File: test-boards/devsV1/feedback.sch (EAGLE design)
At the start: 5 parts, among them IC1 TL074P, Q1 BD139, Q2 BD140

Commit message: feedback schematic transfer done
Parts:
- added C10, C7: 0.1uF, rcl:C-EU025-030X050
- added C11, C8: 22nF, rcl:C-EU025-030X050
- added C12, C9: 220n, rcl:C-EU025-030X050
- added C13, C14: 50n, rcl:C-EU025-030X050
- added C2, C5: 0.33uF, rcl:C-EU025-030X050
- added C3, C6: 1uF, rcl:C-EU025-030X050
- added C4: 2.2 uF, rcl:CPOL-EUE2-5
- added D1, D2, D3, D4, D5, D6, D7: 1N4148, BeagleBone_Blue_R3:DIODE1N4148
- added IC2: 7805L, adafruit:7805L
- added IC3: 7905L, linear:7905L
- added IC4, IC5: TL074P, linear:TL074P
- added JP1, JP2, JP3, JP4, JP5, JP6, JP7: 1x2, pinhead:PINHD-1X2
- added R10, R18: 620K, resistor:R-EU_0207/10
- added R11, R13, R22, R24, R3, R30, R32, R33, R34, R41, R42, R5: 10K, resistor:R-EU_0207/10
- added R12, R14, R17, R4, R6, R9: 1M, resistor:R-EU_0207/10
- added R15, R19, R2, R20, R21, R27, R28, R29, R36, R37, R38, R39, R44, R45, R7: 100K, resistor:R-EU_0207/10
- added R16, R50, R8: 20K, resistor:R-EU_0207/10
- added R23, R31: 300K, resistor:R-EU_0207/10
- added R25, R35, R48, R49: 15K, resistor:R-EU_0207/10
- added R26, R40: 50K, resistor:R-EU_0207/10
- added R43: 150K, resistor:R-EU_0207/10
- added R46: 120K, resistor:R-EU_0207/10
- added R47: 1K, resistor:R-EU_0207/10
- added T1: (no value), transistor:BC337-25-NPN-TO92-CBE
- C1: value (none) -> 2.2 uF
- R1: value (none) -> 100K
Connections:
- new net +12V: JP2.1, Q1.C, R1.1
- new net -12V: JP3.2, Q2.C, R2.1
- new net GND: C1.-, C10.2, C12.1, C2.2, C3.2, C4.-, C5.2, C6.2, C7.2, C9.1, D2.A, D4.A, IC2.GND, IC3.GND, IC4C.+IN, IC4D.+IN, IC5C.+IN, JP1.2, JP2.2, JP3.1, JP4.1, JP5.2, JP6.1, JP7.2, R10.1, R14.1, R15.1, R18.1, R22.2, R24.2, R30.2, R32.2, R39.2, R41.2, R42.2, R49.2, R6.1, R7.1, T1.E
- new net INH: C13.2, IC4D.OUT, JP5.1, R26.1, R47.2
- new net N$1: C1.+, Q1.B, R1.2
- new net N$10: C10.1, IC1B.-IN, R11.2, R12.1
- new net N$11: C9.2, D2.C, IC1D.-IN, R8.2
- new net N$12: D1.C, IC1D.+IN, R10.2, R9.1
- new net N$13: IC1D.OUT, R20.2, R8.1, R9.2
- new net N$14: R36.2, R39.1, R40.1
- new net N$15: IC4A.-IN, R22.1, R23.2
- new net N$16: IC1B.+IN, R13.1, R14.2
- new net N$17: C11.2, D3.A, R15.2
- new net N$18: C12.2, D4.C, IC1C.+IN, R16.2
- new net N$19: IC1C.OUT, R16.1, R17.2, R28.2
- new net N$2: C2.1, IC2.VI, Q1.E
- new net N$20: D3.C, IC1C.-IN, R17.1, R18.2
- new net N$21: D5.A, IC4A.OUT, R23.1
- new net N$22: D5.C, R25.2
- new net N$23: C14.1, IC5C.-IN, R48.1, R49.1, R50.2
- new net N$24: C13.1, IC4D.-IN, R25.1, R26.2, R35.1
- new net N$26: IC4B.+IN, R27.1, R28.1, R29.1, R32.1
- new net N$27: IC5A.-IN, R42.1, R43.2
- new net N$28: D6.A, IC4B.OUT, R31.1
- new net N$29: D6.C, R33.2
- new net N$3: C7.1, IC1A.+IN, R3.2, R4.1
- new net N$30: IC4C.-IN, R33.1, R34.2
- new net N$31: IC4C.OUT, R34.1, R35.2
- new net N$32: IC4B.-IN, R30.1, R31.2
- new net N$33: D7.A, IC5A.OUT, R43.1
- new net N$34: IC5B.+IN, R44.1, T1.C
- new net N$35: IC5B.-IN, R45.1, R46.2
- new net N$36: IC5B.OUT, R46.1, R48.2
- new net N$37: R47.1, T1.B
- new net N$38: C14.2, IC5C.OUT, JP7.1, R50.1
- new net N$4: C4.+, Q2.B, R2.2
- new net N$5: C5.1, IC3.VI, Q2.E
- new net N$6: IC5A.+IN, R36.1, R37.1, R38.1, R41.1
- new net N$7: IC4A.+IN, R19.1, R20.1, R21.1, R24.1
- new net N$8: IC1A.-IN, R5.1, R6.2
- new net N$9: C8.2, D1.A, R7.2
- new net SIGPOST: C11.1, IC1B.OUT, R12.2, R13.2, R21.2, R38.2
- new net SIGPRE: C8.1, IC1A.OUT, R29.2, R37.2, R4.2, R5.2
- new net SOMBRERO: D7.C, JP1.1, R44.2, R45.2
- new net TPOST: JP6.2, R11.1
- new net TPRE: JP4.2, R3.1
- net +5V: now also C3.1, IC2.VO, IC4P.V+, IC5P.V+
- net -5V: now also C6.1, IC3.VO, IC4P.V-, IC5P.V-, R19.2, R27.2, R40.2
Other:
- moved on the sheet: C1, IC1A, IC1B, IC1C, IC1D, Q1, Q2, R1

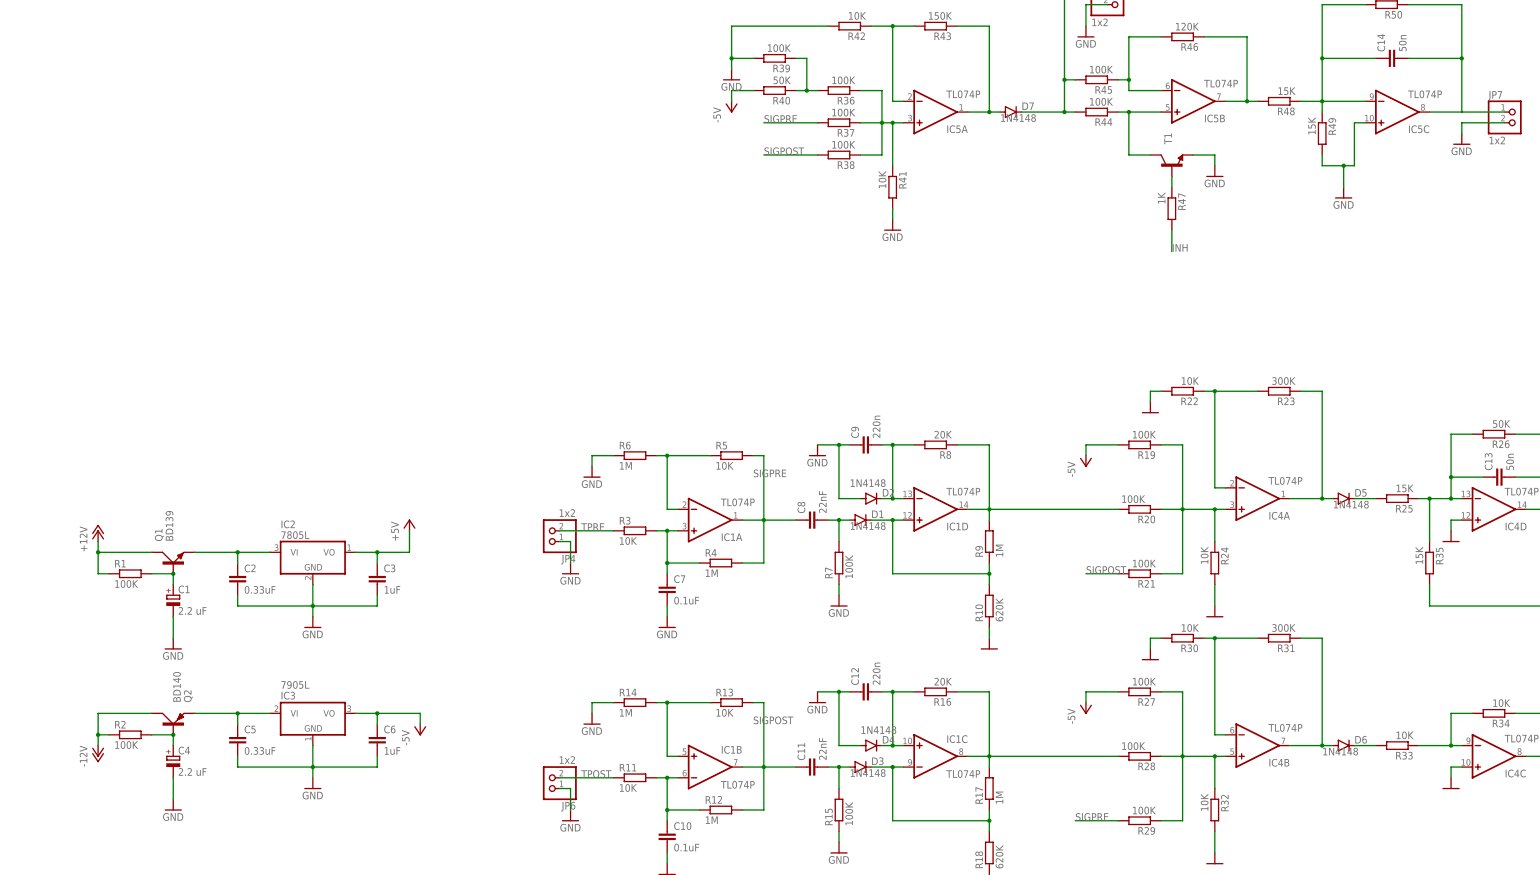
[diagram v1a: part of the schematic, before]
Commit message: finished board routing
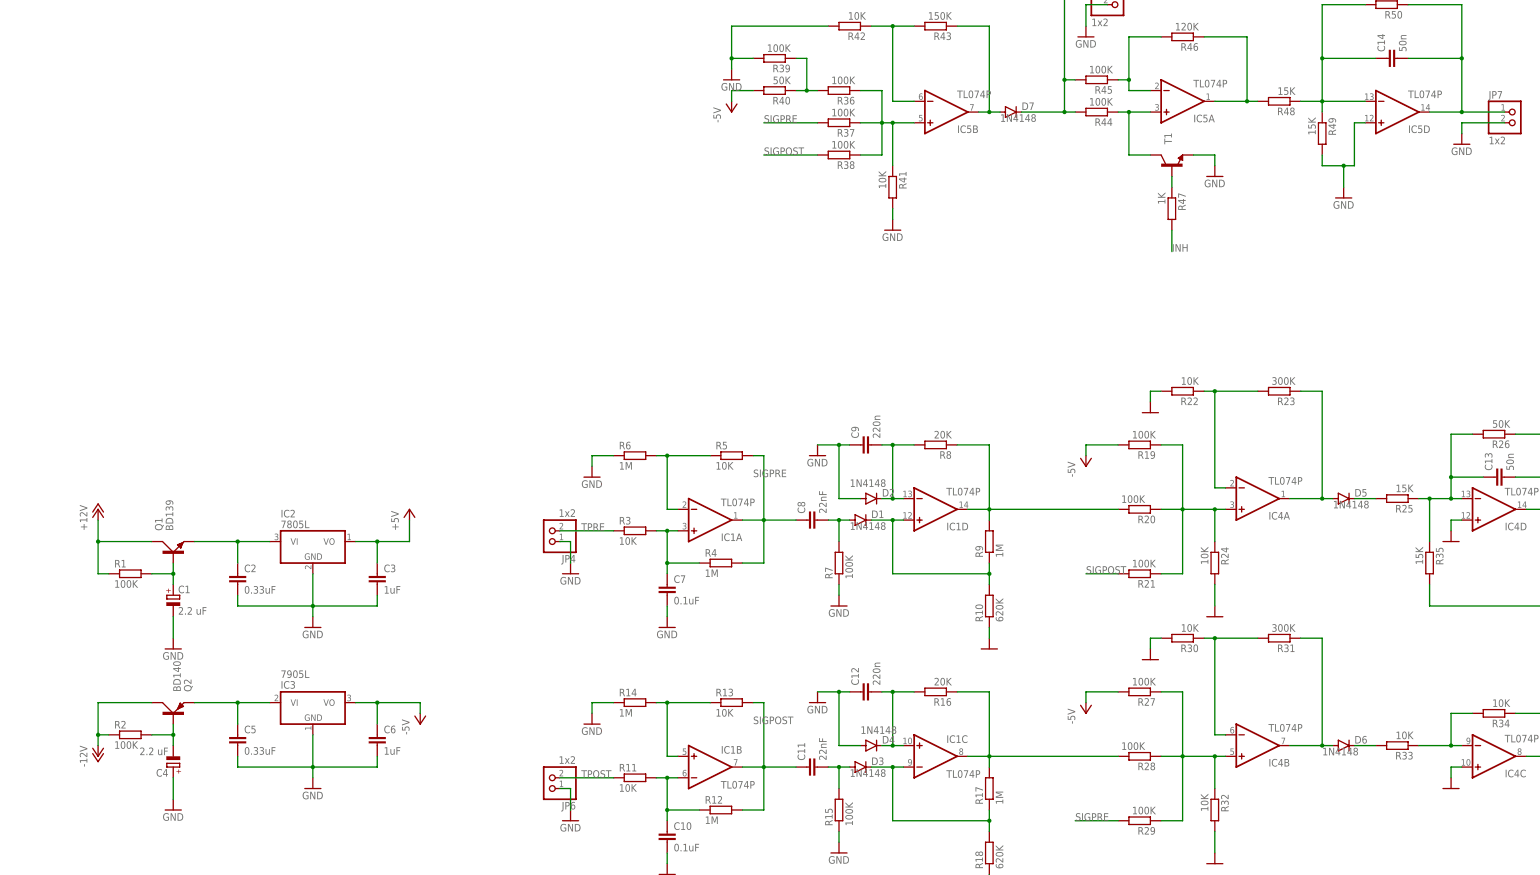
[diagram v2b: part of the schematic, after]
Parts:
- C10, C11, C12, C13, C14, C2, C3, C5, C6, C7, C8, C9: device rcl:C-EU025-030X050 -> rcl:C-EU025-025X050
- IC2: device adafruit:7805L -> linear:7805L
- R1, R10, R11, R12, R13, R14, R15, R16, R17, R18, R19, R2, R20, R21, R22, R23, R24, R25, R26, R27, R28, R29, R3, R30, R31, R32, R33, R34, R35, R36, R37, R38, R4, R40, R41, R44, R45, R46, R47, R48, R49, R5, R50, R6, R7, R8, R9: device resistor:R-EU_0207/10 -> rcl:R-EU_0207/10
- R39, R42, R43: device resistor:R-EU_0207/10 -> rcl:R-EU_0207/10; SPICEPREFIX (none) -> R
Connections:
- net GND: now also C4.+, IC5D.+IN; no longer C4.-, IC5C.+IN
- net N$23: now also IC5D.-IN; no longer IC5C.-IN
- net N$27: now also IC5B.-IN; no longer IC5A.-IN
- net N$33: now also IC5B.OUT; no longer IC5A.OUT
- net N$34: now also IC5A.+IN; no longer IC5B.+IN
- net N$35: now also IC5A.-IN; no longer IC5B.-IN
- net N$36: now also IC5A.OUT; no longer IC5B.OUT
- net N$38: now also IC5D.OUT; no longer IC5C.OUT
- net N$4: now also C4.-; no longer C4.+
- net N$6: now also IC5B.+IN; no longer IC5A.+IN
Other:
- moved on the sheet: C4, IC2, IC3, IC5A, IC5B, Q1, Q2

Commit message: Removed power schema from feedback, and put to separate board
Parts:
- removed C1, C4: 2.2 uF, rcl:CPOL-EUE2-5
- removed C2, C5: 0.33uF, rcl:C-EU025-025X050
- removed C3, C6: 1uF, rcl:C-EU025-025X050
- removed IC2: 7805L, linear:7805L
- removed IC3: 7905L, linear:7905L
- removed JP3: 1x2, pinhead:PINHD-1X2
- removed Q1: BD139, transistor-power:BD139
- removed Q2: BD140, transistor-power:BD140
- removed R1, R2: 100K, rcl:R-EU_0207/10
- JP2: value 1x2 -> (none); device pinhead:PINHD-1X2 -> pinhead:PINHD-1X3
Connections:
- net N$38 renamed HEBB
- removed net +12V: JP2.1, Q1.C, R1.1
- removed net -12V: JP3.2, Q2.C, R2.1
- removed net N$1: C1.+, Q1.B, R1.2
- removed net N$2: C2.1, IC2.VI, Q1.E
- removed net N$4: C4.-, Q2.B, R2.2
- removed net N$5: C5.1, IC3.VI, Q2.E
- net +5V: now also JP2.3; no longer C3.1, IC2.VO
- net -5V: now also JP2.1; no longer C6.1, IC3.VO
- net GND: no longer C1.-, C2.2, C3.2, C4.+, C5.2, C6.2, IC2.GND, IC3.GND, JP3.1
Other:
- moved on the sheet: C10, C11, C12, C13, C14, C7, C8, C9, D1, D2, D3, D4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

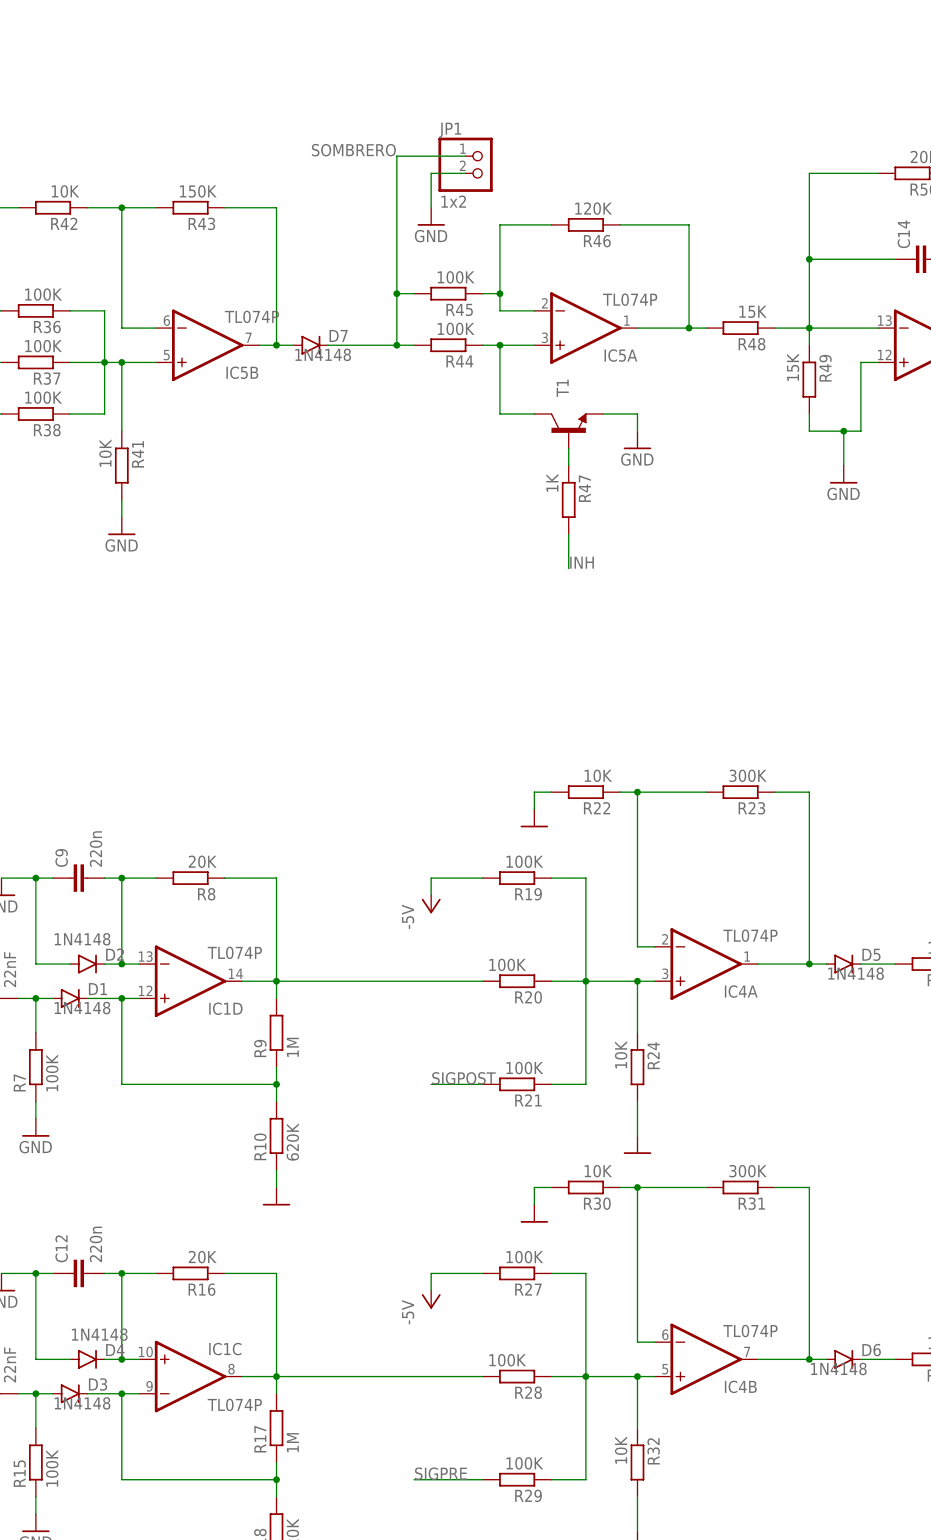
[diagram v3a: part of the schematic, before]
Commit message: reduced size of some boards
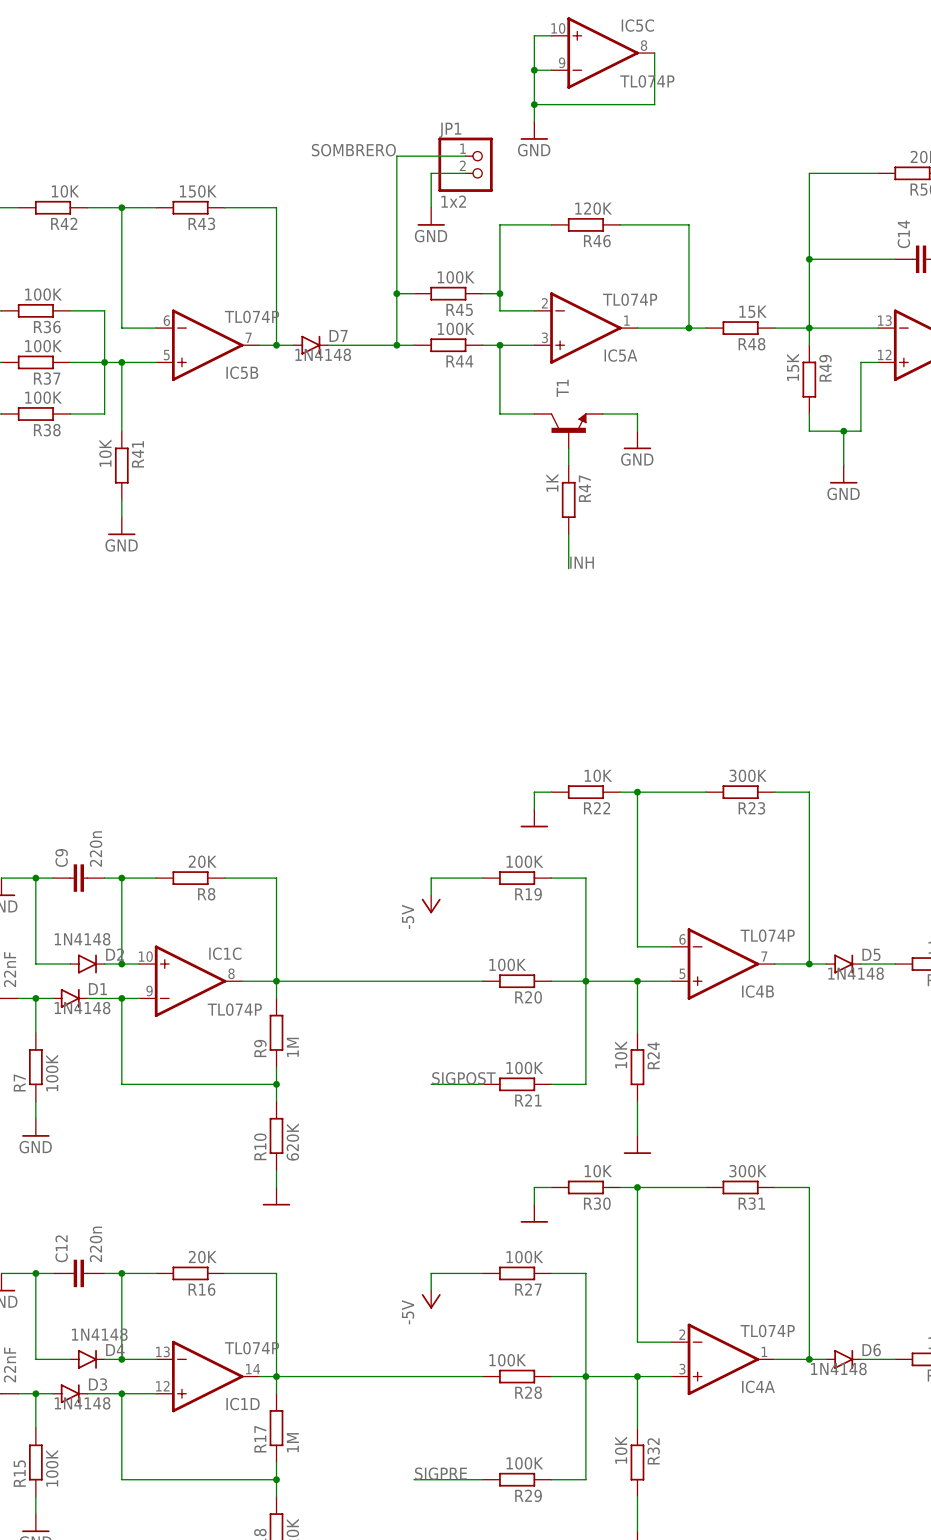
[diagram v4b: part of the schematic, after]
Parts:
- C10, C11, C12, C13, C14, C7, C8, C9: device rcl:C-EU025-025X050 -> resistor:C-EU050-024X044
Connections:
- net GND: now also IC5C.+IN, IC5C.-IN, IC5C.OUT
- net N$11: now also IC1C.+IN; no longer IC1D.-IN
- net N$12: now also IC1C.-IN; no longer IC1D.+IN
- net N$13: now also IC1C.OUT; no longer IC1D.OUT
- net N$15: now also IC4B.-IN; no longer IC4A.-IN
- net N$18: now also IC1D.-IN; no longer IC1C.+IN
- net N$19: now also IC1D.OUT; no longer IC1C.OUT
- net N$20: now also IC1D.+IN; no longer IC1C.-IN
- net N$21: now also IC4B.OUT; no longer IC4A.OUT
- net N$26: now also IC4A.+IN; no longer IC4B.+IN
- net N$28: now also IC4A.OUT; no longer IC4B.OUT
- net N$32: now also IC4A.-IN; no longer IC4B.-IN
- net N$7: now also IC4B.+IN; no longer IC4A.+IN
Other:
- moved on the sheet: IC1C, IC1D, IC4A, IC4B
